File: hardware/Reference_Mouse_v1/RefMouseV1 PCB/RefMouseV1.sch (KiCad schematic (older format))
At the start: 1 part

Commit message: More reference mouse pcb stuff
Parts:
- added TP1, TP2: TEST-POINT3X5, SparkFun-PAD.03X.05, symbol TEST-POINT3X5
- gave numbers to parts that had none: 1
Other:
- note added: "XTAL test point /\nExt. clock override"
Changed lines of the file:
@@
 Sheet 1 2
 Title ""
-Date "26 aug 2013"
+Date "30 aug 2013"
 Rev ""
 Comp ""
@@
 $EndDescr
 $Comp
-L STM32F103RX U?
+L STM32F103RX U2
 U 1 1 521A8AA1
 P 5450 3700
-F 0 "U?" H 5500 3500 60  0000 C CNN
+F 0 "U2" H 5500 3500 60  0000 C CNN
 F 1 "STM32F103RX" H 5500 3800 60  0000 C CNN
 F 2 "~" H 3750 4400 60  0000 C CNN
@@
 $EndComp
 $Sheet
-S 1050 850  650  950
+S 750  700  600  500
 U 521A8DE2
 F0 "RefMouseV1-Power" 50
 F1 "RefMouseV1-Power.sch" 50
-F2 "VBATT_SW" I R 1700 1000 60
-F3 "+3.3V" I R 1700 1200 60
+F2 "VBATT_SW" I R 1350 950 60
+F3 "+3.3V" I R 1350 1100 60
+F4 "VBATT" I R 1350 800 60
 $EndSheet
 $Comp
-L GND #PWR?
+L GND #PWR01
 U 1 1 521ABF7B
 P 4850 1800
-F 0 "#PWR?" H 4850 1800 30  0001 C CNN
+F 0 "#PWR01" H 4850 1800 30  0001 C CNN
 F 1 "GND" H 4850 1730 30  0001 C CNN
 F 2 "" H 4850 1800 60  0000 C CNN
@@
 Wire Wire Line
 	4850 1800 4850 2000
+$Comp
+L TEST-POINT3X5 TP1
+U 1 1 52206320
+P 2700 2550
+F 0 "TP1" H 2800 2650 50  0000 C CNN
+F 1 "TEST-POINT3X5" H 2800 2450 50  0000 C CNN
+F 2 "SparkFun-PAD.03X.05" H 2800 2350 50  0001 C CNN
+F 3 "" H 2700 2550 60  0000 C CNN
+	1    2700 2550
+	1    0    0    -1
+$EndComp
+$Comp
+L TEST-POINT3X5 TP2
+U 1 1 52206458
+P 2400 3150
+F 0 "TP2" H 2500 3250 50  0000 C CNN
+F 1 "TEST-POINT3X5" H 2500 3050 50  0000 C CNN
+F 2 "SparkFun-PAD.03X.05" H 2500 2950 50  0001 C CNN
+F 3 "" H 2400 3150 60  0000 C CNN
+	1    2400 3150
+	1    0    0    -1
+$EndComp
+Text Notes 2100 3400 0    60   ~ 0
+XTAL test point /\nExt. clock override
 $EndSCHEMATC

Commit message: More 3D modeling done!
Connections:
- wire segments 1 -> 3
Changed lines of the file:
@@
 EESchema Schematic File Version 2
-LIBS:power
-LIBS:device
-LIBS:transistors
-LIBS:conn
-LIBS:linear
-LIBS:regul
-LIBS:74xx
-LIBS:cmos4000
-LIBS:adc-dac
-LIBS:memory
-LIBS:xilinx
-LIBS:special
-LIBS:microcontrollers
-LIBS:dsp
-LIBS:microchip
-LIBS:analog_switches
-LIBS:motorola
-LIBS:texas
-LIBS:intel
-LIBS:audio
-LIBS:interface
-LIBS:digital-audio
-LIBS:philips
-LIBS:display
-LIBS:cypress
-LIBS:siliconi
-LIBS:opto
-LIBS:atmel
-LIBS:contrib
-LIBS:valves
 LIBS:stm32f103rx
 LIBS:SparkFun
@@
 Sheet 1 2
 Title ""
-Date "30 aug 2013"
+Date "22 sep 2013"
 Rev ""
 Comp ""
@@
 L GND #PWR01
 U 1 1 521ABF7B
-P 4850 1800
-F 0 "#PWR01" H 4850 1800 30  0001 C CNN
-F 1 "GND" H 4850 1730 30  0001 C CNN
-F 2 "" H 4850 1800 60  0000 C CNN
-F 3 "" H 4850 1800 60  0000 C CNN
-	1    4850 1800
-	-1   0    0    1
+P 4550 2100
+F 0 "#PWR01" H 4550 2100 30  0001 C CNN
+F 1 "GND" H 4550 2030 30  0001 C CNN
+F 2 "" H 4550 2100 60  0000 C CNN
+F 3 "" H 4550 2100 60  0000 C CNN
+	1    4550 2100
+	1    0    0    -1
 $EndComp
-Wire Wire Line
-	4850 1800 4850 2000
 $Comp
 L TEST-POINT3X5 TP1
@@
 Text Notes 2100 3400 0    60   ~ 0
 XTAL test point /\nExt. clock override
+Wire Wire Line
+	4550 2000 4550 1850
+Wire Wire Line
+	4550 1850 4850 1850
+Wire Wire Line
+	4850 1850 4850 2000
 $EndSCHEMATC

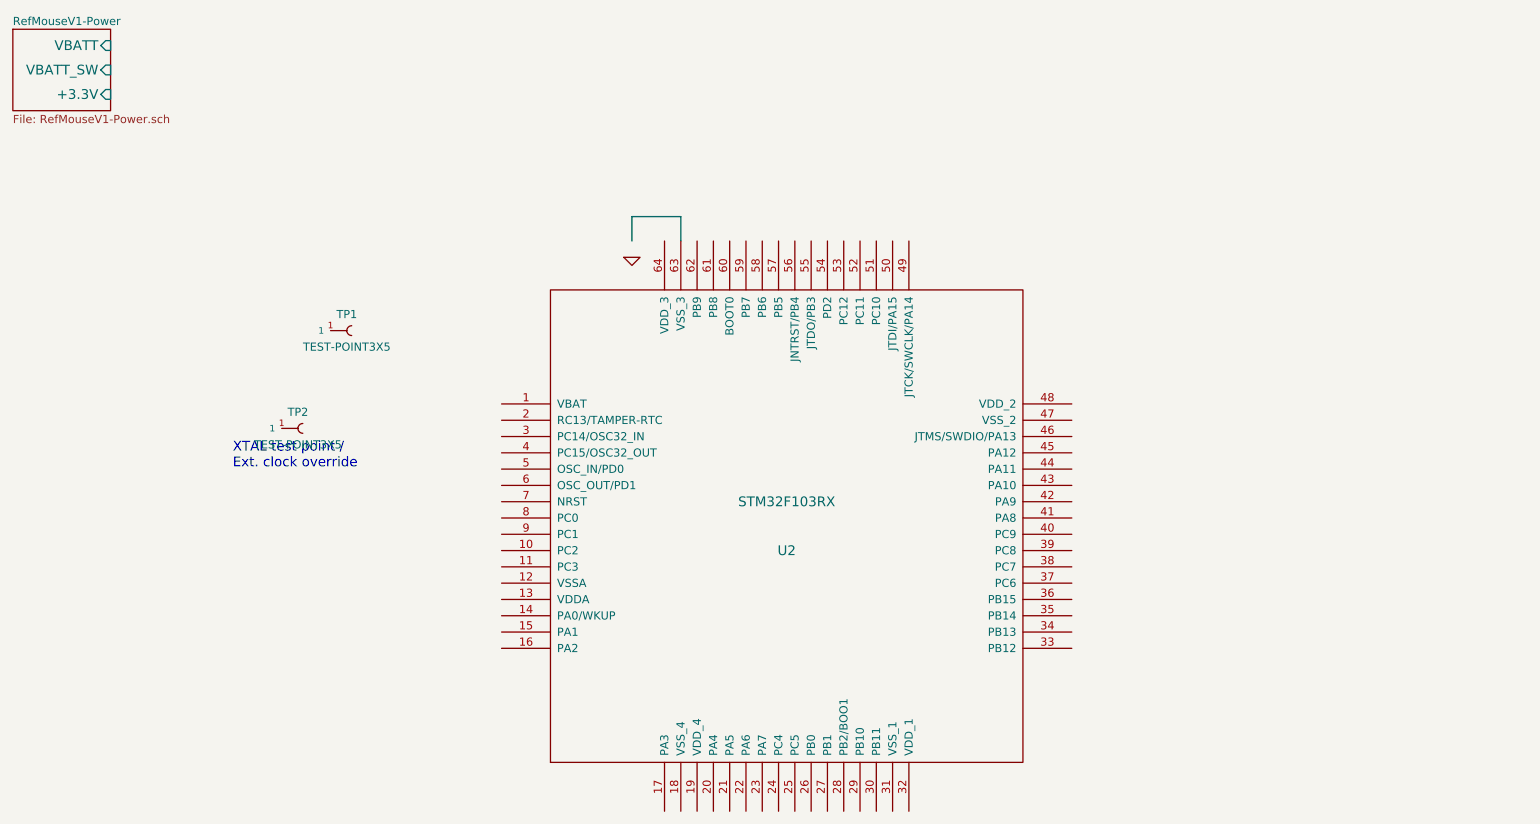
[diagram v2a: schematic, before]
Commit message: Added DRV sch symbol and motor sub-schematic.
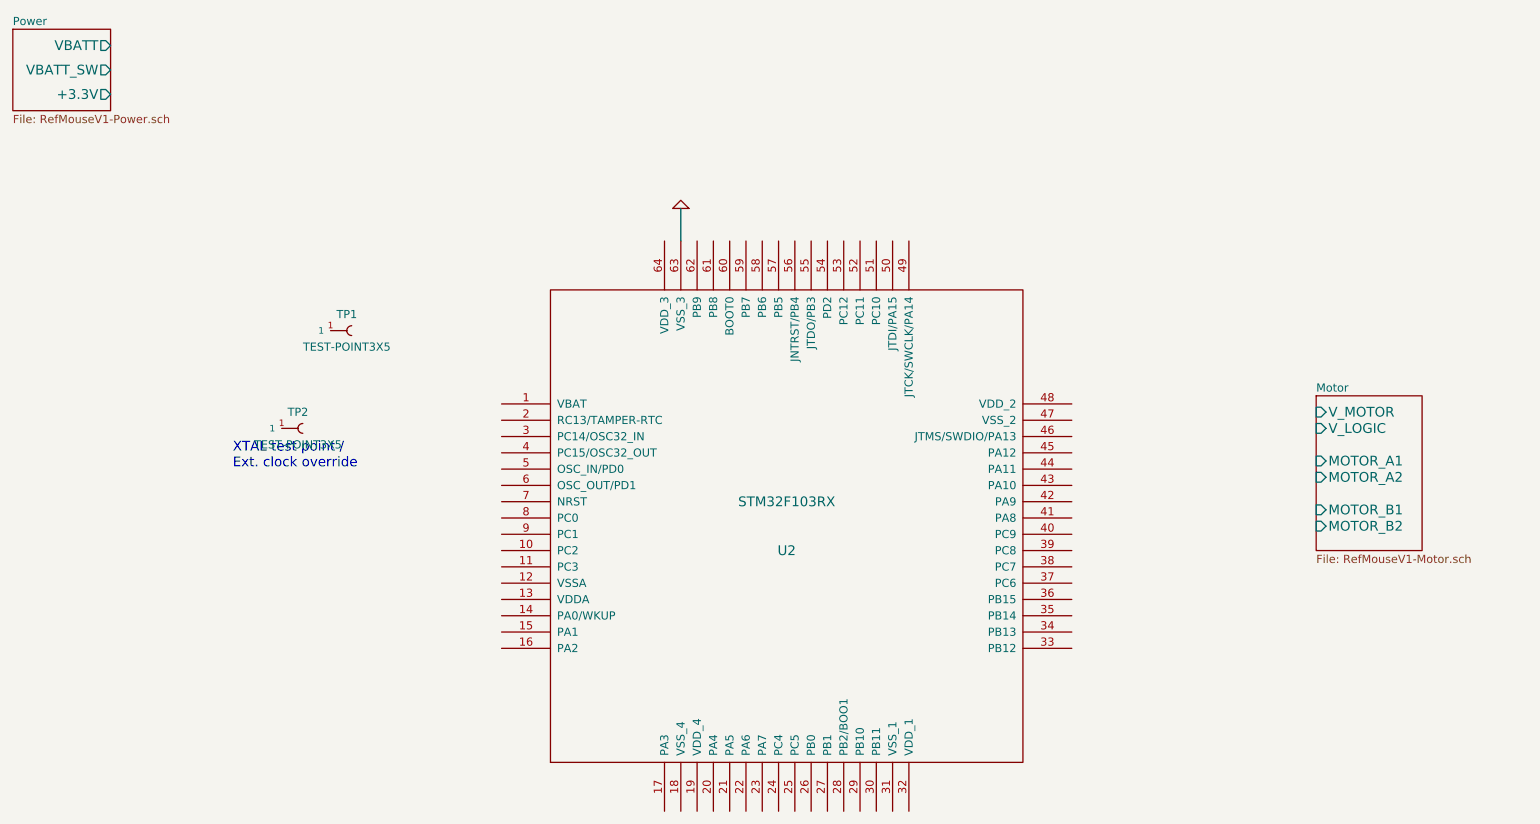
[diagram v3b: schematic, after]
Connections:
- wire segments 3 -> 1
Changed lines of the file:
@@
 EESchema Schematic File Version 2
+LIBS:power
+LIBS:device
+LIBS:transistors
+LIBS:conn
+LIBS:linear
+LIBS:regul
+LIBS:74xx
+LIBS:cmos4000
+LIBS:adc-dac
+LIBS:memory
+LIBS:xilinx
+LIBS:special
+LIBS:microcontrollers
+LIBS:dsp
+LIBS:microchip
+LIBS:analog_switches
+LIBS:motorola
+LIBS:texas
+LIBS:intel
+LIBS:audio
+LIBS:interface
+LIBS:digital-audio
+LIBS:philips
+LIBS:display
+LIBS:cypress
+LIBS:siliconi
+LIBS:opto
+LIBS:atmel
+LIBS:contrib
+LIBS:valves
 LIBS:stm32f103rx
 LIBS:SparkFun
 LIBS:tps6205x
 LIBS:JST-XH-BattBalance
+LIBS:drv8837
 LIBS:RefMouseV1-cache
 EELAYER 27 0
@@
 $Descr USLetter 11000 8500
 encoding utf-8
-Sheet 1 2
+Sheet 1 3
 Title ""
-Date "22 sep 2013"
+Date "5 sep 2013"
 Rev ""
 Comp ""
@@
 S 750  700  600  500
 U 521A8DE2
-F0 "RefMouseV1-Power" 50
+F0 "Power" 50
 F1 "RefMouseV1-Power.sch" 50
-F2 "VBATT_SW" I R 1350 950 60
-F3 "+3.3V" I R 1350 1100 60
-F4 "VBATT" I R 1350 800 60
+F2 "VBATT" O R 1350 800 60
+F3 "VBATT_SW" O R 1350 950 60
+F4 "+3.3V" O R 1350 1100 60
 $EndSheet
 $Comp
 L GND #PWR01
 U 1 1 521ABF7B
-P 4550 2100
-F 0 "#PWR01" H 4550 2100 30  0001 C CNN
-F 1 "GND" H 4550 2030 30  0001 C CNN
-F 2 "" H 4550 2100 60  0000 C CNN
-F 3 "" H 4550 2100 60  0000 C CNN
-	1    4550 2100
-	1    0    0    -1
+P 4850 1800
+F 0 "#PWR01" H 4850 1800 30  0001 C CNN
+F 1 "GND" H 4850 1730 30  0001 C CNN
+F 2 "" H 4850 1800 60  0000 C CNN
+F 3 "" H 4850 1800 60  0000 C CNN
+	1    4850 1800
+	-1   0    0    1
 $EndComp
+Wire Wire Line
+	4850 1800 4850 2000
 $Comp
 L TEST-POINT3X5 TP1
@@
 Text Notes 2100 3400 0    60   ~ 0
 XTAL test point /\nExt. clock override
-Wire Wire Line
-	4550 2000 4550 1850
-Wire Wire Line
-	4550 1850 4850 1850
-Wire Wire Line
-	4850 1850 4850 2000
+$Sheet
+S 8750 2950 650  950
+U 5227CDAA
+F0 "Motor" 50
+F1 "RefMouseV1-Motor.sch" 50
+F2 "MOTOR_A1" I L 8750 3350 60
+F3 "MOTOR_A2" I L 8750 3450 60
+F4 "MOTOR_B1" I L 8750 3650 60
+F5 "MOTOR_B2" I L 8750 3750 60
+F6 "V_LOGIC" I L 8750 3150 60
+F7 "V_MOTOR" I L 8750 3050 60
+$EndSheet
 $EndSCHEMATC
